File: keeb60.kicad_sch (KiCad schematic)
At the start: 123 parts, among them K000 Esc, K001 1, K002 2, K003 3, K004 4, K005 5, K006 6, K007 7, K008 8, K009 9, K010 0, K011 _, K012 =, K013 Backspace, K100 Tab, K101 Q, K102 W, K103 E, K104 R, K105 T, K106 Y, K107 U, K108 I, K109 O, K110 P, K111 [, K112 ], K113 |, K200 Caps Lock, K201 A, K202 S, K203 D, K204 F, K205 G, K206 H, K207 J, K208 K, K209 L, K210 ;, K211 ,, K213 Enter, K300 Shift, K302 Z, K303 X, K304 C, K305 V, K306 B, K307 N, K308 M, K309 ,, K310 ., K311 /, K313 Shift, K400 Ctrl, K401 Option, K402 Command, K406 Space, K410 Command, K411 Option, K412 Function, K413 Ctrl, U1 ProMicro

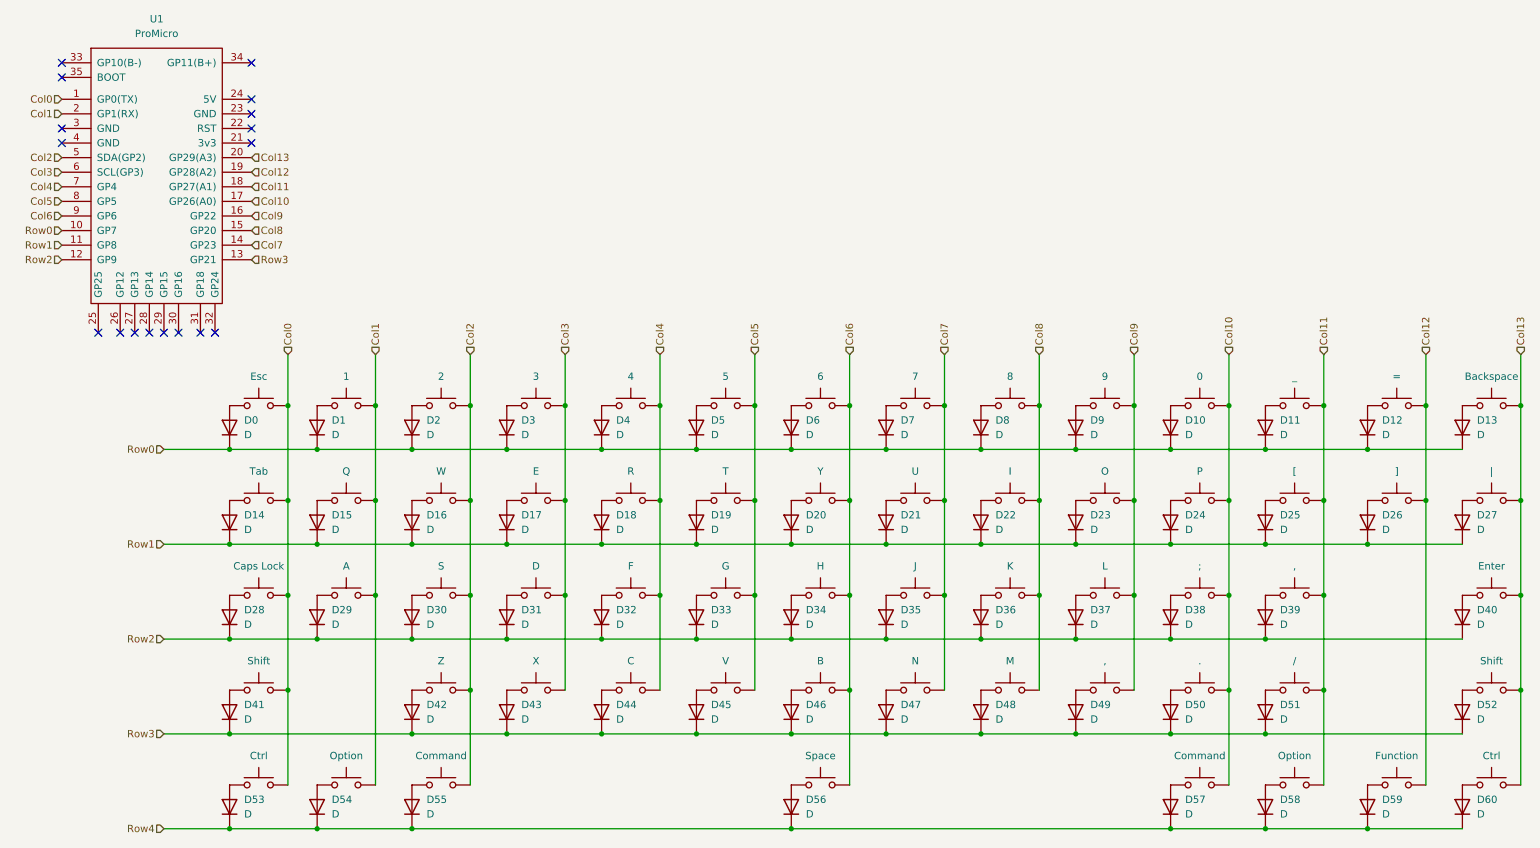
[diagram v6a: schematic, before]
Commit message: Move to 13 columns
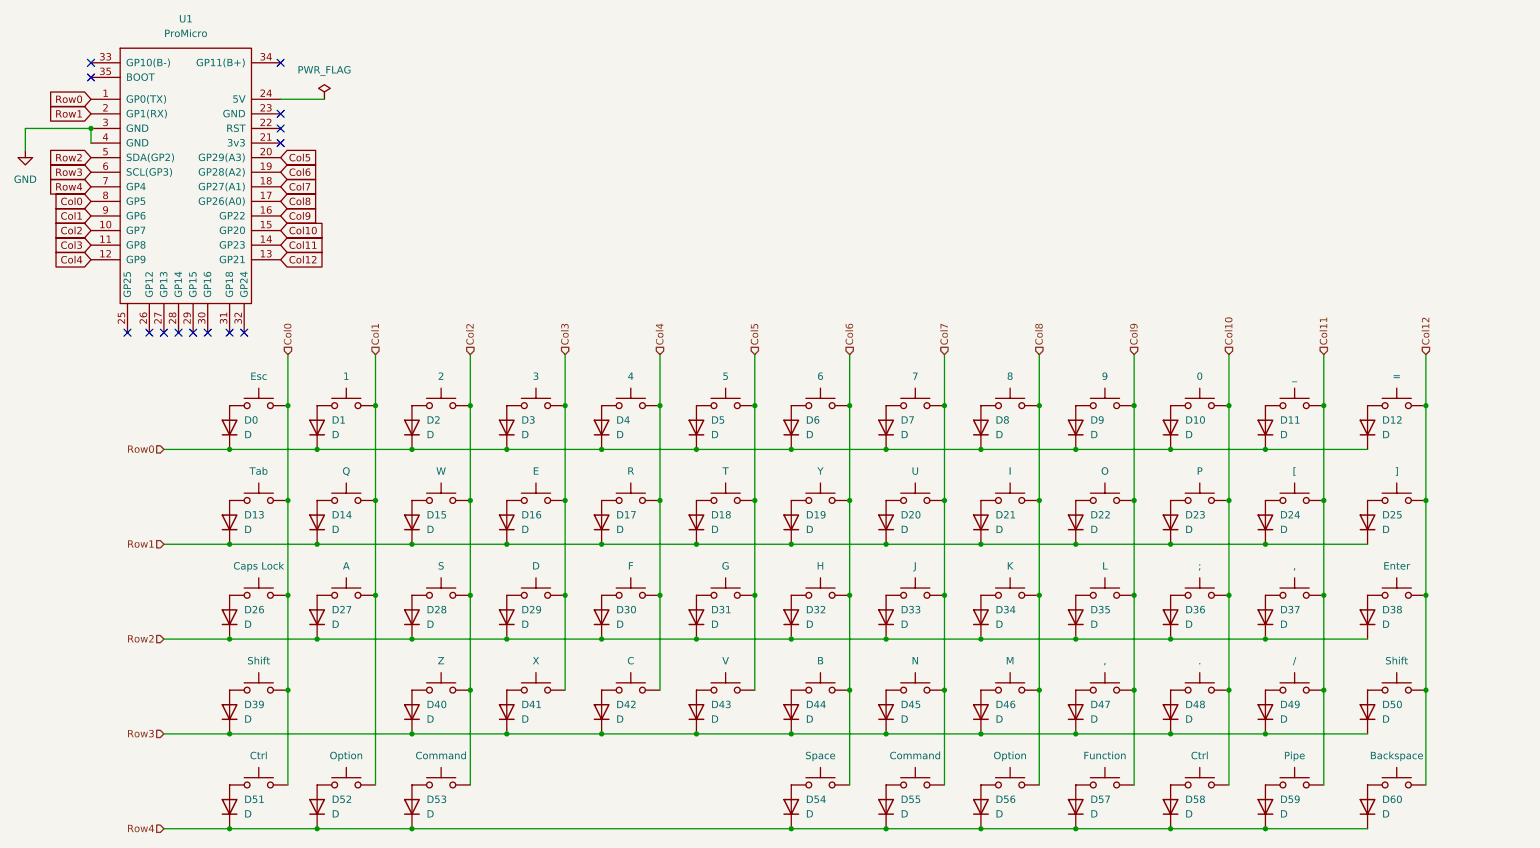
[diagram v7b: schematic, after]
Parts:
- removed D27: D, Diode_SMD:D_SOD-123, symbol Device:D
- added D59: D, Diode_SMD:D_SOD-123, symbol Device:D
- K113: value | -> Pipe
- renumbered D14 to D13, D15 to D14, D16 to D15, D17 to D16, D18 to D17, D19 to D18, D20 to D19, D21 to D20, D22 to D21, D23 to D22, D24 to D23, D25 to D24, D26 to D25, D28 to D26, D29 to D27, D30 to D28, D31 to D29, D32 to D30, D33 to D31, D34 to D32, D35 to D33, D36 to D34, D37 to D35, D38 to D36, D39 to D37, D40 to D38, D41 to D39, D42 to D40, D43 to D41, D44 to D42, D45 to D43, D46 to D44, D47 to D45, D48 to D46, D49 to D47, D50 to D48, D51 to D49, D52 to D50, D53 to D51, D54 to D52, D55 to D53, D56 to D54, D57 to D55, D58 to D56, D59 to D57, D60 to D58, D13 to D60
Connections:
- net Col0: now also U1.8 (GP5); no longer U1.1 (GP0(TX))
- net Col1: now also U1.9 (GP6); no longer U1.2 (GP1(RX))
- net Col10: now also K413.2, U1.15 (GP20); no longer K410.2, U1.17 (GP26(A0))
- net Col11: now also K113.2, U1.14 (GP23); no longer K411.2, U1.18 (GP27(A1))
- net Col12: now also K013.2, K213.2, K313.2, U1.13 (GP21); no longer K412.2, U1.19 (GP28(A2))
- net Col2: now also U1.10 (GP7); no longer U1.5 (SDA(GP2))
- net Col3: now also U1.11 (GP8); no longer U1.6 (SCL(GP3))
- net Col4: now also U1.12 (GP9); no longer U1.7 (GP4)
- net Col5: now also U1.20 (GP29(A3)); no longer U1.8 (GP5)
- net Col6: now also U1.19 (GP28(A2)); no longer U1.9 (GP6)
- net Col7: now also K410.2, U1.18 (GP27(A1)); no longer U1.14 (GP23)
- net Col8: now also K411.2, U1.17 (GP26(A0)); no longer U1.15 (GP20)
- net Col9: now also K412.2
- net Row0: now also U1.1 (GP0(TX)); no longer D60.1 (K), U1.10 (GP7)
- net Row1: now also U1.2 (GP1(RX)); no longer U1.11 (GP8)
- net Row2: now also U1.5 (SDA(GP2)); no longer U1.12 (GP9)
- net Row3: now also U1.6 (SCL(GP3)); no longer U1.13 (GP21)
- net Row4: now also D60.1 (K), U1.7 (GP4), D59.1 (K)
- net at K113.1: now also D59.2 (A)
- net GND: now reaches U1.3 (GND)
- net GND: now also U1.4 (GND)
- removed net Col13: K013.2, K113.2, K213.2, K313.2, K413.2, U1.20 (GP29(A3))
- no-connect marks 17 -> 14
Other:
- moved on the sheet: D38, D50, D55, D56, D57, D58, D60, U1
